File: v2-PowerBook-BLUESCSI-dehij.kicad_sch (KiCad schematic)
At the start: 41 parts, among them J1 Micro_SD_Card, J2 Conn_02x20_Odd_Even, U1 YAAJ_BluePill_Part_Like

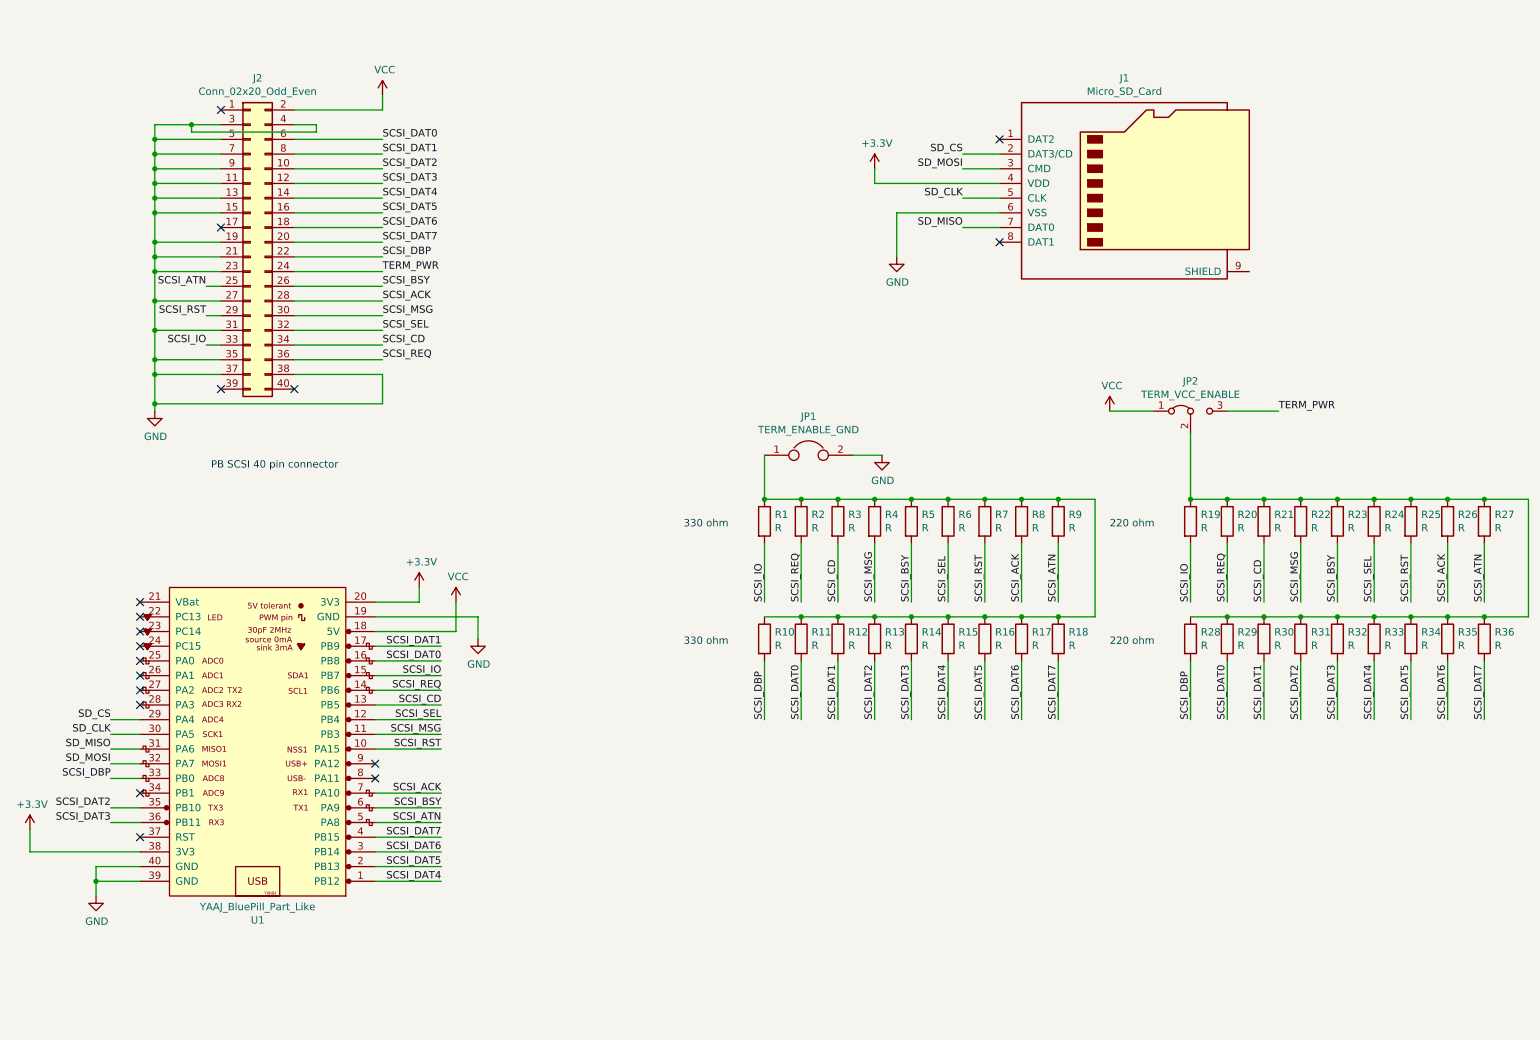
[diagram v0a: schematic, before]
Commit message: Moved resistors to 2 lines added silk screen rounded corners changed sd card
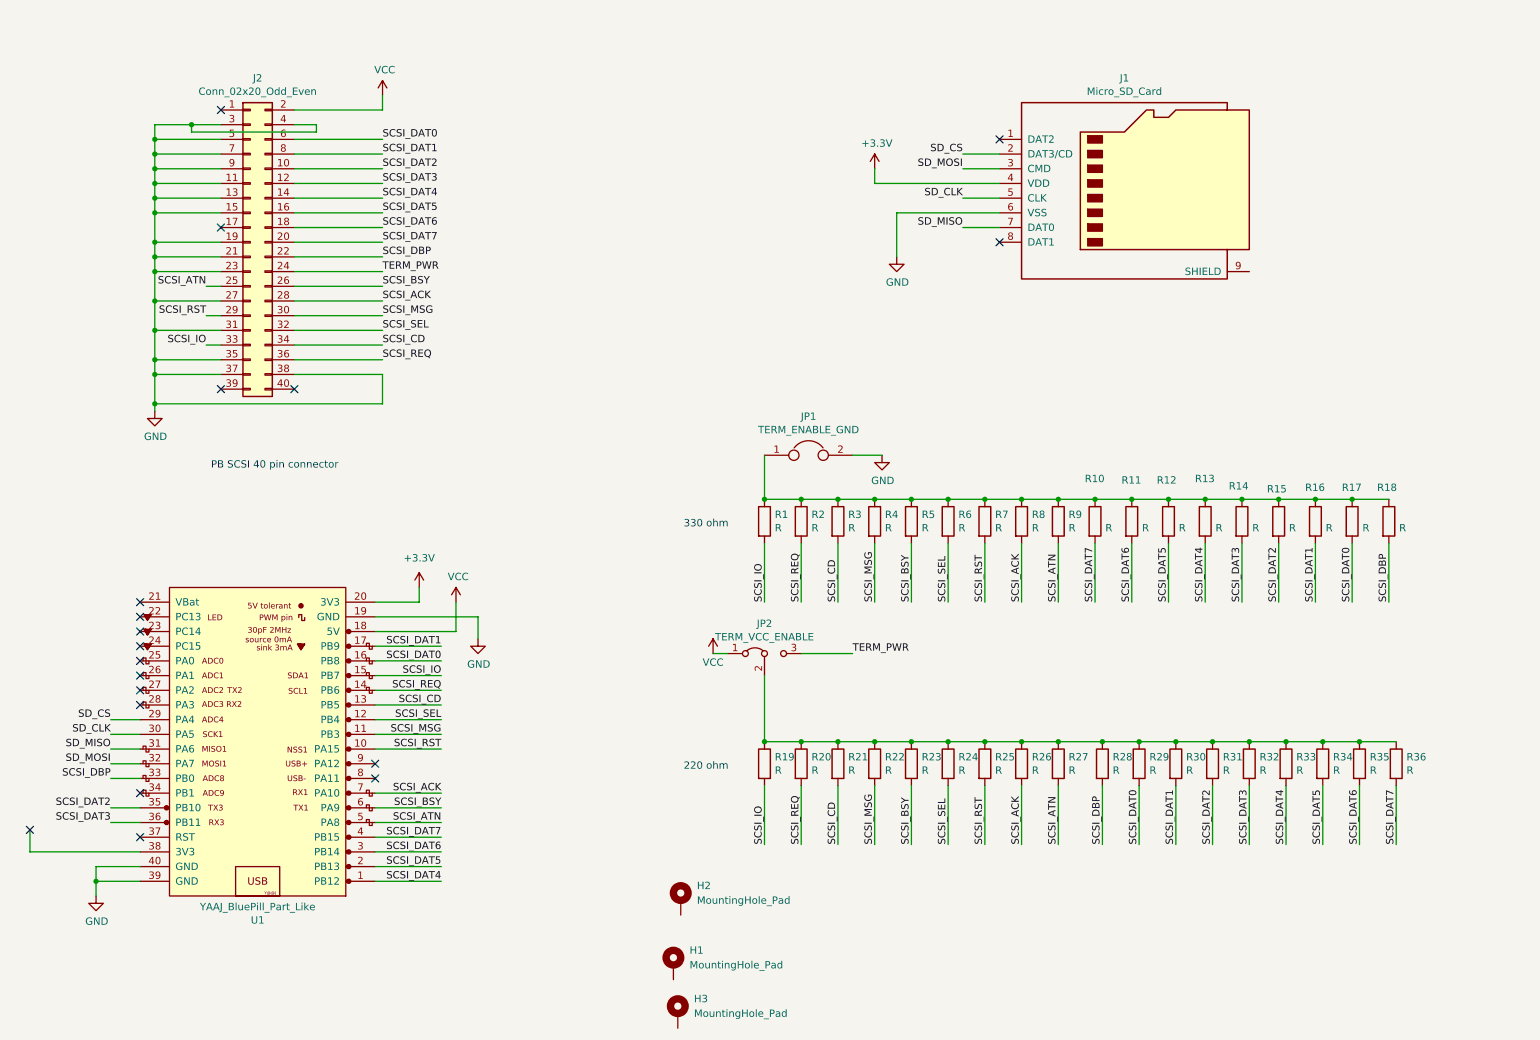
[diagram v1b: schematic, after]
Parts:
- added H1, H2, H3: MountingHole_Pad, MountingHole:MountingHole_2.5mm_Pad_Via, symbol Mechanical:MountingHole_Pad
- J1: footprint Other footprints:Conn_uSDcard -> Connector_Card:microSD_HC_Molex_104031-0811
- JP1: footprint Jumper:SolderJumper-2_P1.3mm_Bridged_Pad1.0x1.5mm -> Connector_PinSocket_2.54mm:PinSocket_1x02_P2.54mm_Vertical
- JP2: footprint Jumper:SolderJumper-3_P1.3mm_Bridged12_Pad1.0x1.5mm_NumberLabels -> Connector_PinSocket_2.54mm:PinSocket_1x03_P2.54mm_Vertical
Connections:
- net +3V3: no longer U1.38 (3V3)
- net SCSI_DAT0: now also R17.2; no longer R11.2
- net SCSI_DAT1: now also R16.2; no longer R12.2
- net SCSI_DAT2: now also R15.2; no longer R13.2
- net SCSI_DAT4: now also R13.2; no longer R15.2
- net SCSI_DAT5: now also R12.2; no longer R16.2
- net SCSI_DAT6: now also R11.2; no longer R17.2
- net SCSI_DAT7: now also R10.2; no longer R18.2
- net SCSI_DBP: now also R18.2; no longer R10.2
- no-connect marks 18 -> 19
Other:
- moved on the sheet: JP2, R10, R11, R12, R13, R14, R15, R16, R17, R18, R19, R20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

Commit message: Tonys Updates
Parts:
- H1, H2, H3: value MountingHole_Pad -> (none); footprint MountingHole:MountingHole_2.5mm_Pad_Via -> (none)
- J1: value Micro_SD_Card -> (none); footprint Connector_Card:microSD_HC_Molex_104031-0811 -> (none); LCSC (none) -> C585350
- J2: value Conn_02x20_Odd_Even -> (none); footprint Connector_PinSocket_2.00mm:PinSocket_2x20_P2.00mm_Vertical -> (none)
- JP1: value TERM_ENABLE_GND -> (none); footprint Connector_PinSocket_2.54mm:PinSocket_1x02_P2.54mm_Vertical -> (none); symbol v2-PowerBook-BLUESCSI-dehij-rescue:Jumper-Device -> Jumper:Jumper_2_Bridged
- JP2: value TERM_VCC_ENABLE -> (none); footprint Connector_PinSocket_2.54mm:PinSocket_1x03_P2.54mm_Vertical -> (none)
- R1, R10, R11, R12, R13, R14, R15, R16, R17, R18, R2, R3, R4, R5, R6, R7, R8, R9: value R -> (none); footprint Resistor_SMD:R_1206_3216Metric_Pad1.30x1.75mm_HandSolder -> (none); LCSC (none) -> C17930
- R19, R20, R21, R22, R23, R24, R25, R26, R27, R28, R29, R30, R31, R32, R33, R34, R35, R36: value R -> (none); footprint Resistor_SMD:R_1206_3216Metric_Pad1.30x1.75mm_HandSolder -> (none); LCSC (none) -> C17957
- U1: value YAAJ_BluePill_Part_Like -> (none); footprint Footprints:YAAJ_BluePill_2 -> (none)
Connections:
- net GND: now also H1.1, H2.1, H3.1, J1.9 (SHIELD)
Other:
- moved on the sheet: H1, H2, H3
